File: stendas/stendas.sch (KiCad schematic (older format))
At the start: 44 parts, among them J1 RA8875, J17 MB SLAVE, J2 EXT1, J22 MB MASTER, J3 EXT2, J5 EXT, J6 Service, M1 STM32F4-Disco, Q1 BC817, U1 ST485B, U2 ST485B

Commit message: pirma plokstes versija
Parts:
- added C12: 27p, symbol capacitors:C_100n_0805_X7R
- added C2, C21: 0.1, Capacitor_SMD:C_0805_2012Metric, symbol capacitors:C_100n_0805_X7R
- added R13, R14: 4.7k, Resistor_SMD:R_0805_2012Metric, symbol Device:R
- added U3: 24LC32, Package_SO:SOIC-8_3.9x4.9mm_P1.27mm, symbol Memory_EEPROM:24LC32
- renumbered C2 to C1, C12 to C11, C1 to C15, C11 to C16, C15 to C17, C16 to C18, C17 to C19, C18 to C20, C19 to C22, J17 to J1, J22 to J2, J1 to J3, J3 to J4, J2 to J7, R6 to R2, R2 to R3, R3 to R4, R7 to R5, R8 to R6, R4 to R7, R9 to R8, R5 to R9
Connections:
- net 3VDC: now also R13.1, R14.1, U3.8 (VCC)
- net DS_DATA: now also J7.11 (Pin_11)
- net GND: now also C12.1, C2.1, C21.1, U3.1 (A0), U3.2 (A1), U3.3 (A2), U3.4 (GND), U3.7 (WP)
- net PWM1: now also J7.8 (Pin_8)
- net PWM2: now also J7.7 (Pin_7)
- net PWM3: now also J7.10 (Pin_10)
- net PWM4: now also J7.9 (Pin_9)
- net U4DE: now also M1.24 (PB2)
- net U5DE: now also M1.81 (PD3)
- net ~CS: now also C12.2
- net ADC_CH3: now reaches M1.13 (PA3)
- net ADC_CH2: now reaches M1.14 (PA2)
- net VDD: now reaches M1.3 (VDD)
- net VDD: now also M1.4 (VDD), C2.2
- net BUZ: now reaches M1.69 (PB8)
- net at M1.72 (VDD): now also C21.2
- net SCL: now reaches M1.73 (PB6)
- net SCL: now also J7.16 (Pin_16), R14.2, U3.6 (SCL)
- net SDA: now reaches M1.74 (PB7)
- net SDA: now also J7.17 (Pin_17), R13.2, U3.5 (SDA)
- net TEST_OUT: now reaches M1.90 (PA15)
- net ADC1 renamed ADC_CH10
- net ADC2 renamed ADC_CH11
- net ADC3 renamed ADC_CH12
- net ADC4 renamed ADC_CH13
- net ADC5 renamed ADC_CH14
- net ADC6 renamed ADC_CH15
- net ADC7 renamed ADC_CH8
- net ADC8 renamed ADC_CH9
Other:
- moved on the sheet: BZ1, D1, Q1, R11, R12

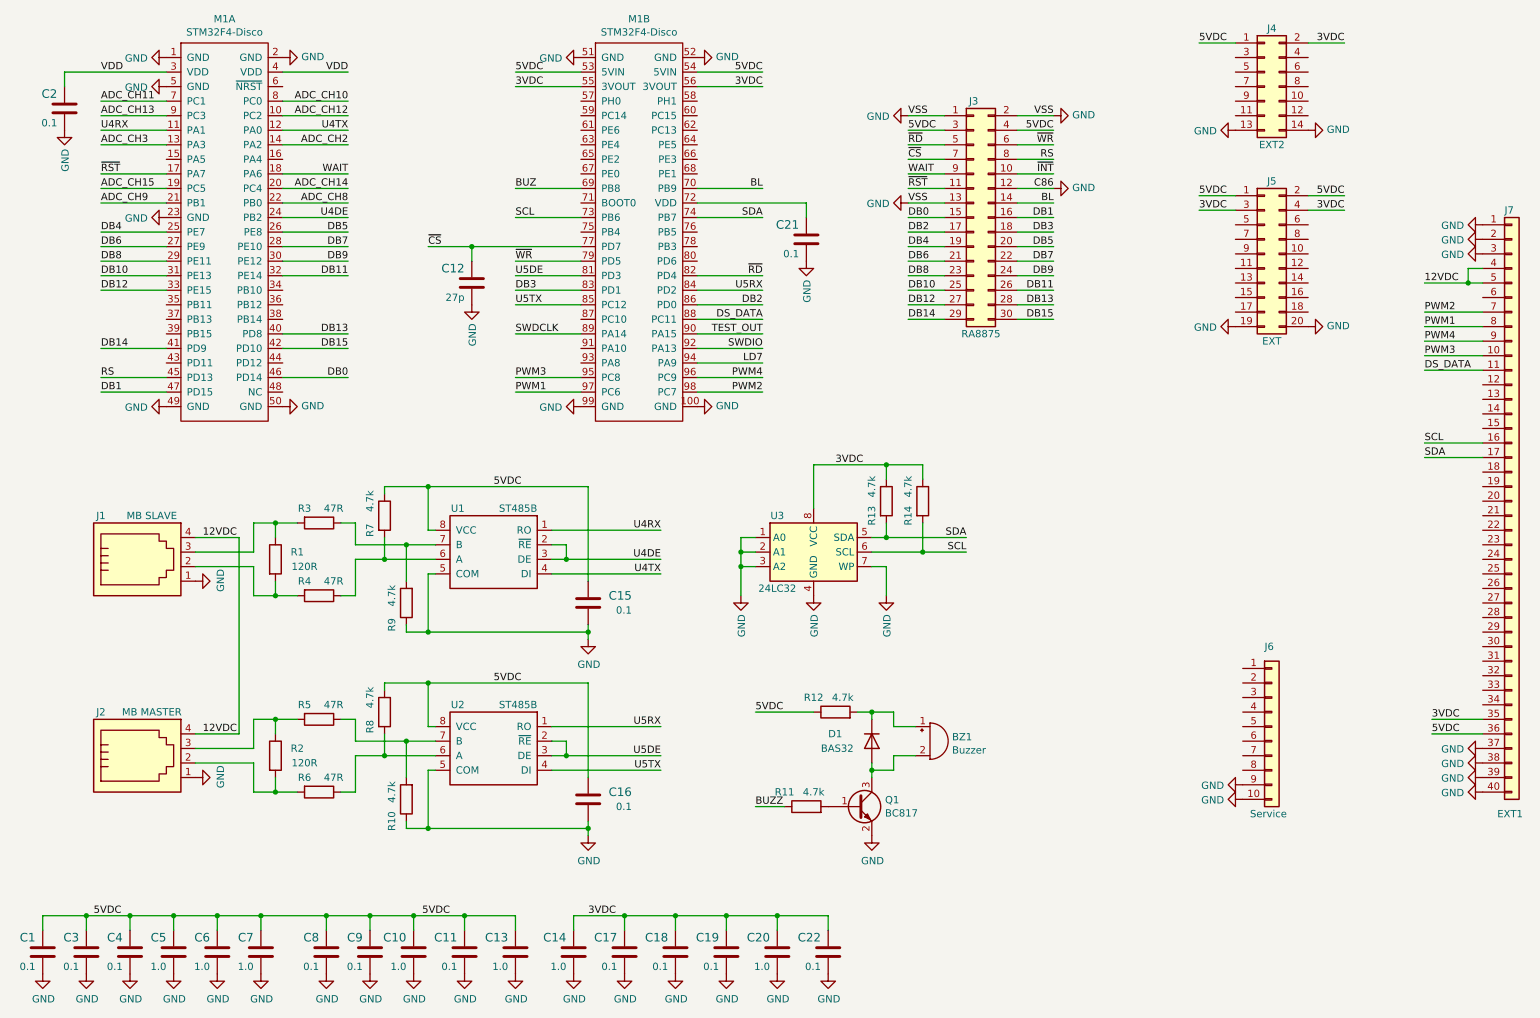
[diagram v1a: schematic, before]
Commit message: remapinti pinai - plokste pritaikyta darbui su sd-card
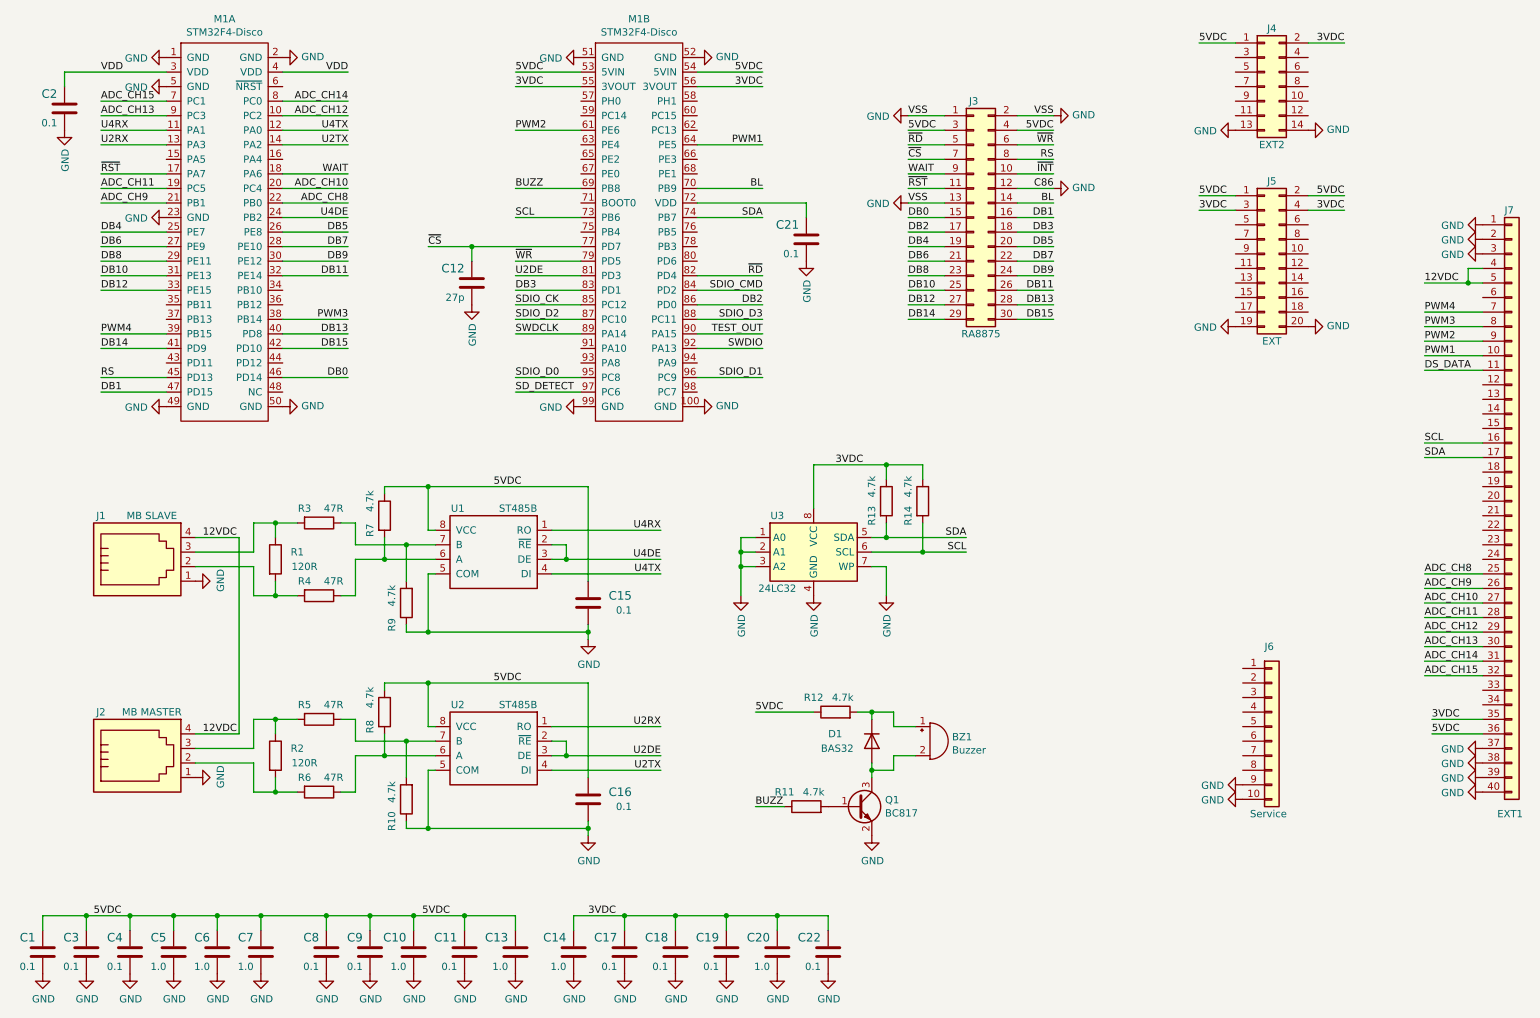
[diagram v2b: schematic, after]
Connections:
- net BUZ is gone; now on net BUZZ: M1.69 (PB8)
- net ADC_CH10: now also J7.27 (Pin_27), M1.20 (PC4); no longer M1.8 (PC0)
- net ADC_CH11: now also J7.28 (Pin_28), M1.19 (PC5); no longer M1.7 (PC1)
- net ADC_CH12: now also J7.29 (Pin_29)
- net ADC_CH13: now also J7.30 (Pin_30)
- net ADC_CH14: now also J7.31 (Pin_31), M1.8 (PC0); no longer M1.20 (PC4)
- net ADC_CH15: now also J7.32 (Pin_32), M1.7 (PC1); no longer M1.19 (PC5)
- net ADC_CH8: now also J7.25 (Pin_25)
- net ADC_CH9: now also J7.26 (Pin_26)
- net DS_DATA: no longer M1.88 (PC11)
- net PWM1: now also J7.10 (Pin_10), M1.64 (PE5); no longer J7.8 (Pin_8), M1.97 (PC6)
- net PWM2: now also J7.9 (Pin_9), M1.61 (PE6); no longer J7.7 (Pin_7), M1.98 (PC7)
- net PWM3: now also J7.8 (Pin_8), M1.38 (PB14); no longer J7.10 (Pin_10), M1.95 (PC8)
- net PWM4: now also J7.7 (Pin_7), M1.39 (PB15); no longer J7.9 (Pin_9), M1.96 (PC9)
- net SDIO_D2: now reaches M1.87 (PC10)
- net ADC_CH2 renamed U2TX
- net U2TX: now also U2.4 (DI)
- net ADC_CH3 renamed U2RX
- net U2RX: now also U2.1 (RO)
- net LD7: no longer names the net of M1.94 (PA9)
- net U5DE renamed U2DE
- net U5RX renamed SDIO_CMD
- net SDIO_CMD: no longer U2.1 (RO)
- net U5TX renamed SDIO_CK
- net SDIO_CK: no longer U2.4 (DI)
- new net SDIO_D0: M1.95 (PC8)
- new net SDIO_D1: M1.96 (PC9)
- new net SDIO_D3: M1.88 (PC11)
- new net SD_DETECT: M1.97 (PC6)
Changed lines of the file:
@@
 Wire Wire Line
 	4450 2800 4000 2800
-Text Label 4000 2800 0    50   ~ 0
-U5TX
 Wire Wire Line
 	5250 2700 5700 2700
-Text Label 5700 2700 2    50   ~ 0
-U5RX
 $Comp
 L power:GND #PWR029
@@
 Text Label 5700 1300 2    50   ~ 0
 3VDC
-Wire Wire Line
-	5250 3200 5700 3200
-Text Label 5700 3200 2    50   ~ 0
-LD7
 $Comp
 L Connector_Generic:Conn_02x07_Odd_Even J4
@@
 Connection ~ 4500 6400
 Text Label 5000 5700 2    50   ~ 0
-U5RX
+U2RX
 Text Label 5000 6000 2    50   ~ 0
-U5TX
+U2TX
 Text Label 5000 5900 2    50   ~ 0
-U5DE
+U2DE
 Wire Wire Line
 	2350 5650 2500 5650
@@
 BUZZ
 Wire Wire Line
-	4450 3400 4000 3400
-Wire Wire Line
-	5250 3400 5700 3400
-Wire Wire Line
 	4450 3300 4000 3300
 Wire Wire Line
 	5250 3300 5700 3300
-Text Label 4000 3400 0    50   ~ 0
+Text Label 5700 1700 2    50   ~ 0
 PWM1
-Text Label 5700 3400 2    50   ~ 0
+Text Label 4000 1600 0    50   ~ 0
 PWM2
-Text Label 4000 3300 0    50   ~ 0
+Text Label 2850 2900 2    50   ~ 0
 PWM3
-Text Label 5700 3300 2    50   ~ 0
+Text Label 1150 3000 0    50   ~ 0
 PWM4
 Text Label 5700 3100 2    50   ~ 0
@@
 SWDCLK
 Text Label 5700 2900 2    50   ~ 0
-DS_DATA
+SDIO_D3
 Wire Wire Line
 	5250 2900 5700 2900
@@
 Wire Wire Line
 	2400 1500 2850 1500
-Text Label 2850 1400 2    50   ~ 0
+Text Label 2850 2000 2    50   ~ 0
 ADC_CH10
-Text Label 1150 1400 0    50   ~ 0
+Text Label 1150 2000 0    50   ~ 0
 ADC_CH11
 Text Label 2850 1500 2    50   ~ 0
@@
 Wire Wire Line
 	2400 2000 2850 2000
-Text Label 2850 2000 2    50   ~ 0
+Text Label 2850 1400 2    50   ~ 0
 ADC_CH14
-Text Label 1150 2000 0    50   ~ 0
+Text Label 1150 1400 0    50   ~ 0
 ADC_CH15
 Wire Wire Line
@@
 	4450 2000 4000 2000
 Text Label 4000 2000 0    50   ~ 0
-BUZ
-Wire Wire Line
-	1600 1700 1150 1700
-Wire Wire Line
-	2400 1700 2850 1700
-Text Label 2850 1700 2    50   ~ 0
-ADC_CH2
-Text Label 1150 1700 0    50   ~ 0
-ADC_CH3
+BUZZ
 Wire Wire Line
 	4450 2200 4000 2200
@@
 Wire Wire Line
 	10650 2850 10250 2850
+Text Label 10250 3150 0    50   ~ 0
+PWM1
+Text Label 10250 3050 0    50   ~ 0
+PWM2
 Text Label 10250 2950 0    50   ~ 0
-PWM1
+PWM3
 Text Label 10250 2850 0    50   ~ 0
-PWM2
-Text Label 10250 3150 0    50   ~ 0
-PWM3
-Text Label 10250 3050 0    50   ~ 0
 PWM4
 Wire Wire Line
 	2400 2200 2850 2200
+Wire Wire Line
+	5250 1700 5700 1700
+Wire Wire Line
+	4450 1600 4000 1600
+Wire Wire Line
+	2400 2900 2850 2900
+Wire Wire Line
+	1600 3000 1150 3000
 Text Label 2850 2200 2    50   ~ 0
 U4DE
+Text Label 5700 2700 2    50   ~ 0
+SDIO_CMD
+Text Label 4000 2800 0    50   ~ 0
+SDIO_CK
+Wire Wire Line
+	4450 2900 4000 2900
+Text Label 4000 2900 0    50   ~ 0
+SDIO_D2
+Text Label 5700 3300 2    50   ~ 0
+SDIO_D1
+Text Label 4000 3300 0    50   ~ 0
+SDIO_D0
+Wire Wire Line
+	4450 3400 4000 3400
+Text Label 4000 3400 0    50   ~ 0
+SD_DETECT
+Wire Wire Line
+	2400 1700 2850 1700
+Wire Wire Line
+	1600 1700 1150 1700
+Text Label 1150 1700 0    50   ~ 0
+U2RX
+Text Label 2850 1700 2    50   ~ 0
+U2TX
 Wire Wire Line
 	4450 2600 4000 2600
 Text Label 4000 2600 0    50   ~ 0
-U5DE
+U2DE
+Wire Wire Line
+	10650 4650 10250 4650
+Wire Wire Line
+	10650 4750 10250 4750
+Wire Wire Line
+	10650 4850 10250 4850
+Wire Wire Line
+	10650 4950 10250 4950
+Wire Wire Line
+	10650 5050 10250 5050
+Wire Wire Line
+	10650 5150 10250 5150
+Wire Wire Line
+	10650 5250 10250 5250
+Wire Wire Line
+	10650 5350 10250 5350
+Text Label 10250 4650 0    50   ~ 0
+ADC_CH8
+Text Label 10250 4750 0    50   ~ 0
+ADC_CH9
+Text Label 10250 4850 0    50   ~ 0
+ADC_CH10
+Text Label 10250 4950 0    50   ~ 0
+ADC_CH11
+Text Label 10250 5050 0    50   ~ 0
+ADC_CH12
+Text Label 10250 5150 0    50   ~ 0
+ADC_CH13
+Text Label 10250 5250 0    50   ~ 0
+ADC_CH14
+Text Label 10250 5350 0    50   ~ 0
+ADC_CH15
 $EndSCHEMATC
